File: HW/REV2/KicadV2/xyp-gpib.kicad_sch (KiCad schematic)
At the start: 25 parts, among them J1 USB_C_Receptacle_USB2.0, SW1 SW_Push, U1 ATmega32U4-MU, Y1 CX2016DB16000D0WZRC1

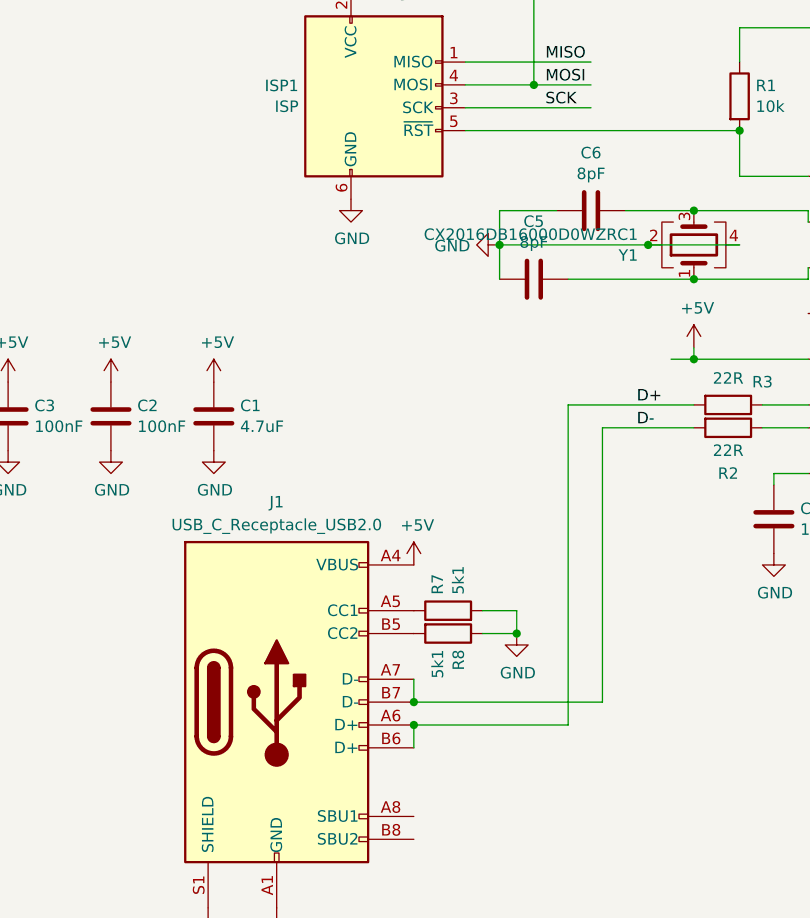
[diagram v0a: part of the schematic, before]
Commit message: GPIBee is available
- GPIBee availability / link sharing
- Adding more "proven to work"devices.
- Some BOM adjustments (was raised as Issue and this addresses it)
- Share a beautifully done project: Zandan Khan's XyphroLabs-USBGpib-DMM4050
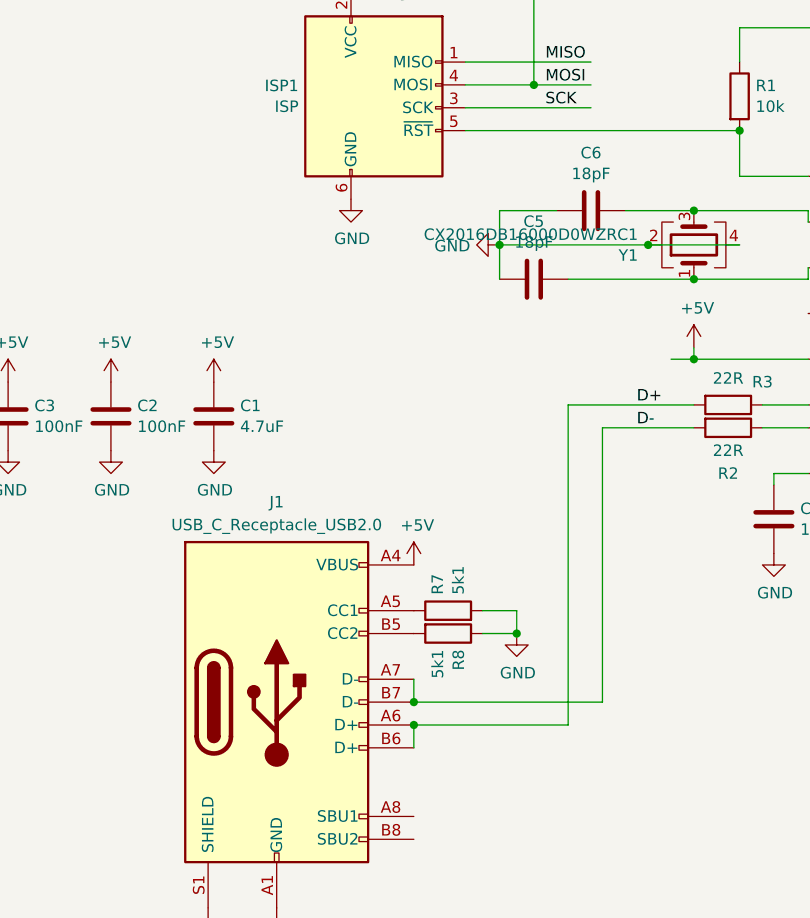
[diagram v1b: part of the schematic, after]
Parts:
- C5, C6: value 8pF -> 18pF
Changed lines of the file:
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@@
 (kicad_sch
-	(version 20231120)
+	(version 20250114)
 	(generator "eeschema")
-	(generator_version "8.0")
+	(generator_version "9.0")
 	(paper "A4")
+	(text "PF0 = GND\nfor HW revision detection"
+		(exclude_from_sim no)
+		(at 170.18 121.92 0)
+		(effects
+			(font
+				(size 1.27 1.27)
+			)
+			(justify left bottom)
+		)
+	)
+	(text "use REN pin as 12 MHz clock output to FE1.1s"
+		(exclude_from_sim no)
+		(at 165.735 74.93 0)
+		(effects
+			(font
+				(size 1.27 1.27)
+			)
+			(justify left bottom)
+		)
+	)
 	(junction
 		(at 118.11 57.15)
@@
 		)
 	)
-	(text "PF0 = GND\nfor HW revision detection"
-		(exclude_from_sim no)
-		(at 170.18 121.92 0)
-		(effects
-			(font
-				(size 1.27 1.27)
-			)
-			(justify left bottom)
-		)
-	)
-	(text "use REN pin as 12 MHz clock output to FE1.1s"
-		(exclude_from_sim no)
-		(at 165.735 74.93 0)
-		(effects
-			(font
-				(size 1.27 1.27)
-			)
-			(justify left bottom)
-		)
-	)
 	(label "DIO3"
 		(at 214.63 86.36 0)
-		(fields_autoplaced yes)
 		(effects
 			(font
@@
 	(label "D+"
 		(at 106.68 87.63 0)
-		(fields_autoplaced yes)
 		(effects
 			(font
@@
 	(label "DAV"
 		(at 158.75 77.47 0)
-		(fields_autoplaced yes)
 		(effects
 			(font
@@
 	(label "EOI"
 		(at 214.63 91.44 0)
-		(fields_autoplaced yes)
 		(effects
 			(font
@@
 	(label "D-"
 		(at 106.68 90.17 0)
-		(fields_autoplaced yes)
 		(effects
 			(font
@@
 	(label "NRFD"
 		(at 214.63 96.52 0)
-		(fields_autoplaced yes)
 		(effects
 			(font
@@
 	(label "DIO8"
 		(at 246.38 88.9 0)
-		(fields_autoplaced yes)
 		(effects
 			(font
@@
 	(label "DAV"
 		(at 214.63 93.98 0)
-		(fields_autoplaced yes)
 		(effects
 			(font
@@
 	(label "NDAC"
 		(at 214.63 99.06 0)
-		(fields_autoplaced yes)
 		(effects
 			(font
@@
 	(label "DIO6"
 		(at 157.48 105.41 0)
-		(fields_autoplaced yes)
 		(effects
 			(font
@@
 	(label "MISO"
 		(at 96.52 49.53 0)
-		(fields_autoplaced yes)
 		(effects
 			(font
@@
 	(label "DIO7"
 		(at 246.38 86.36 0)
-		(fields_autoplaced yes)
 		(effects
 			(font
@@
 	(label "DIO5"
 		(at 246.38 81.28 0)
-		(fields_autoplaced yes)
 		(effects
 			(font
@@
 	(label "SRQ"
 		(at 214.63 104.14 0)
-		(fields_autoplaced yes)
 		(effects
 			(font
@@
 	(label "ATN"
 		(at 158.75 133.35 0)
-		(fields_autoplaced yes)
 		(effects
 			(font
@@
 	(label "REN"
 		(at 246.38 91.44 0)
-		(fields_autoplaced yes)
 		(effects
 			(font
@@
 	(label "SCK"
 		(at 96.52 54.61 0)
-		(fields_autoplaced yes)
 		(effects
 			(font
@@
 	(label "IFC"
 		(at 214.63 101.6 0)
-		(fields_autoplaced yes)
 		(effects
 			(font
@@
 	(label "NDAC"
 		(at 158.75 87.63 0)
-		(fields_autoplaced yes)
 		(effects
 			(font
@@
 	(label "DIO5"
 		(at 157.48 102.87 0)
-		(fields_autoplaced yes)
 		(effects
 			(font
@@
 	(label "ATN"
 		(at 214.63 106.68 0)
-		(fields_autoplaced yes)
 		(effects
 			(font
@@
 	(label "DIO1"
 		(at 214.63 81.28 0)
-		(fields_autoplaced yes)
 		(effects
 			(font
@@
 	(label "MOSI"
 		(at 165.1 67.31 0)
-		(fields_autoplaced yes)
 		(effects
 			(font
@@
 	(label "EOI"
 		(at 158.75 72.39 0)
-		(fields_autoplaced yes)
 		(effects
 			(font
@@
 	(label "DIO2"
 		(at 158.75 95.25 0)
-		(fields_autoplaced yes)
 		(effects
 			(font
@@
 	(label "DIO6"
 		(at 246.38 83.82 0)
-		(fields_autoplaced yes)
 		(effects
 			(font
@@
 	(label "DIO2"
 		(at 214.63 83.82 0)
-		(fields_autoplaced yes)
 		(effects
 			(font
@@
 	(label "DIO4"
 		(at 214.63 88.9 0)
-		(fields_autoplaced yes)
 		(effects
 			(font
@@
 	(label "SRQ"
 		(at 158.75 135.89 0)
-		(fields_autoplaced yes)
 		(effects
 			(font
@@
 	(label "DIO3"
 		(at 158.75 97.79 0)
-		(fields_autoplaced yes)
 		(effects
 			(font
@@
 	(label "DIO4"
 		(at 158.75 100.33 0)
-		(fields_autoplaced yes)
 		(effects
 			(font
@@
 	(label "DIO8"
 		(at 157.48 110.49 0)
-		(fields_autoplaced yes)
 		(effects
 			(font
@@
 	(label "MOSI"
 		(at 96.52 52.07 0)
-		(fields_autoplaced yes)
 		(effects
 			(font
@@
 	(label "SCK"
 		(at 165.1 64.77 0)
-		(fields_autoplaced yes)
 		(effects
 			(font
@@
 	(label "REN"
 		(at 158.75 74.93 0)
-		(fields_autoplaced yes)
 		(effects
 			(font
@@
 	(label "DIO1"
 		(at 158.75 92.71 0)
-		(fields_autoplaced yes)
 		(effects
 			(font
@@
 	(label "IFC"
 		(at 158.75 115.57 0)
-		(fields_autoplaced yes)
 		(effects
 			(font
@@
 	(label "DIO7"
 		(at 157.48 107.95 0)
-		(fields_autoplaced yes)
 		(effects
 			(font
@@
 	(label "MISO"
 		(at 165.1 69.85 0)
-		(fields_autoplaced yes)
 		(effects
 			(font
@@
 	(label "NRFD"
 		(at 158.75 85.09 0)
-		(fields_autoplaced yes)
 		(effects
 			(font
@@
 			)
 		)
-		(property "Value" "8pF"
+		(property "Value" "18pF"
 			(at 95.25 69.5706 90)
 			(effects
@@
 			)
 		)
-		(property "Value" "8pF"
+		(property "Value" "18pF"
 			(at 101.6 61.9506 90)
 			(effects
@@
 		)
 	)
+	(embedded_fonts no)
 )
